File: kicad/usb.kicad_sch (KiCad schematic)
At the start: 46 parts, among them J2 HX PZ2.54-2X5P TP, U2 FSUSB42MUX, U3 USB2514B-I/M2, U4 AP22653W6-7, U5 TPD4EUSB30DQAR, U6 TPD4EUSB30DQAR, U7 TPD4EUSB30DQAR, X1 24MHz

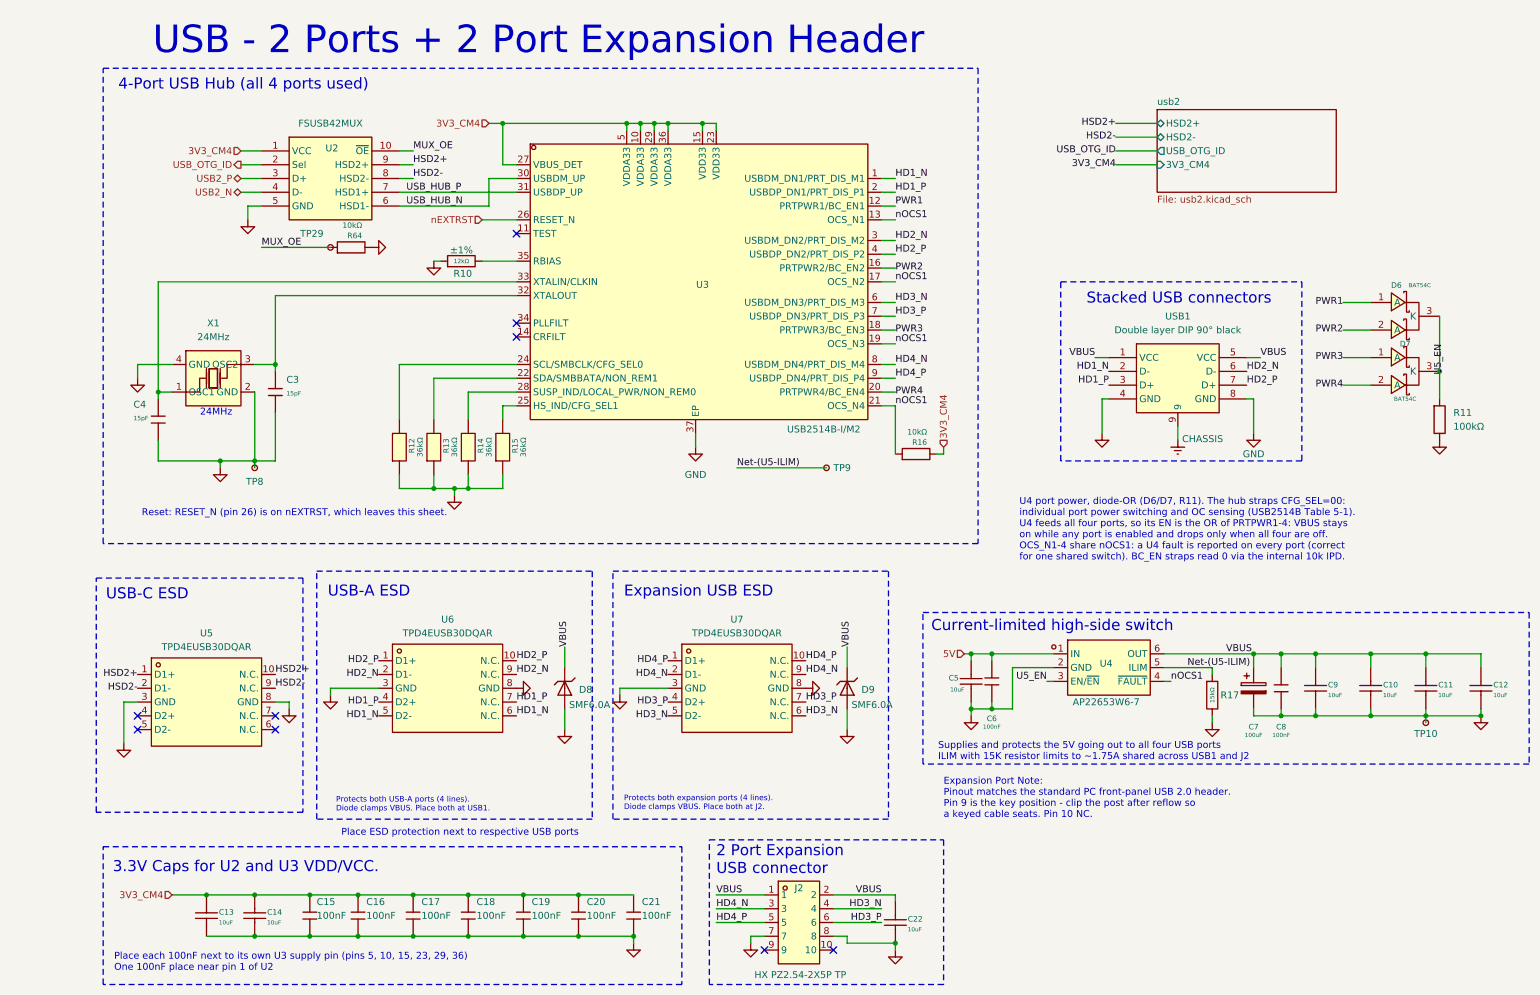
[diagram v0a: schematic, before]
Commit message: PCB: swap GPS and USB areas, drop J2 and hub ports 3/4, remap J4
- Remove expansion header J2 with C22, U7, D9 and D7; disable USB2514B
  ports 3 and 4 with 10k pull-ups (R94-R97) on their D-/D+ straps.
- Remap J4 GPIO pins so they route to the CM4 connector without
  crossovers (schematic labels, notes and PCB pad nets).
- Add decoupling caps C84 (U10) and C85 (U17); add HUB_CTRL net class.
- Move USB (USB1, USBC1, hub) to the top edge and GPS (U12, CN1, J7) to
  the bottom-left; R4/R5 move with the GPS group. First-pass placement,
  all USB and GPS copper removed for manual routing.
- Relabel bottom-edge silk text for the SMA connectors.
- README and usb-power sim note updated for the two-port hub.
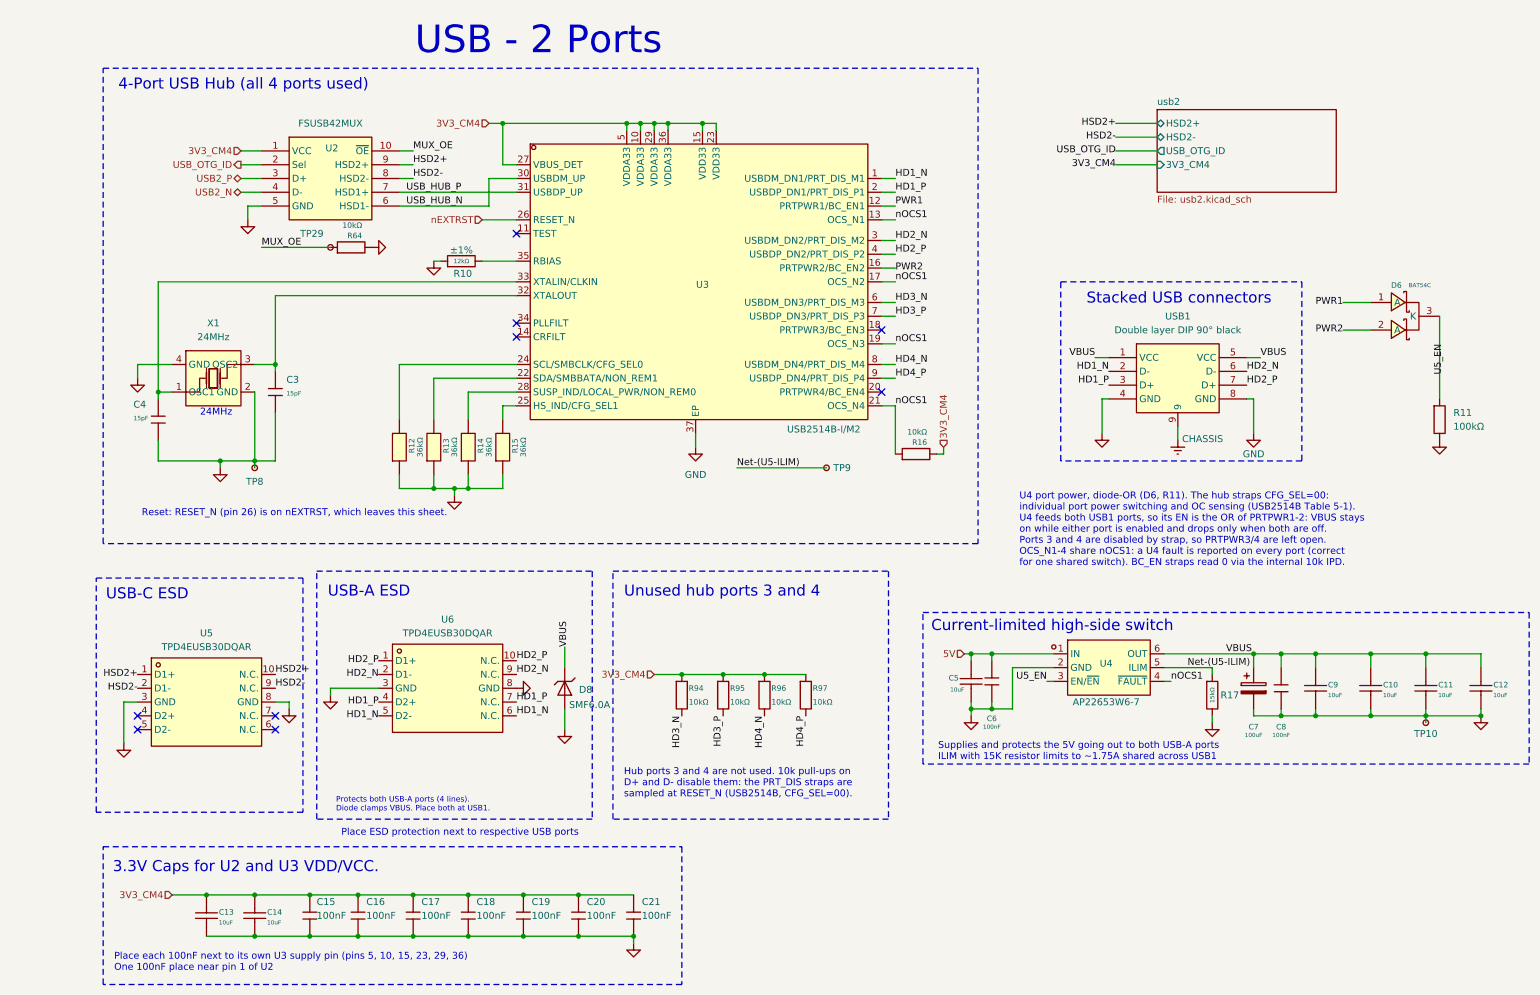
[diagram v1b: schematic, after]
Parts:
- removed C22: 10uF, MyPartsIPC:CAPC2012X145N, symbol MyParts:CL21B106KPQNNNE
- removed D7: BAT54C, MyPartsIPC:SOT95P280X110-3N, symbol MyParts:BAT54C
- removed D9: SMF6.0A, MyPartsIPC:SODFL3718X110N, symbol MyParts:SMF6.0A
- removed J2: HX PZ2.54-2X5P TP, MyParts:HDR-SMD_10P-P2.54-V-M-R2-C5-LS7.5, symbol MyParts:HXPZ2.54-2X5PTP
- removed U7: TPD4EUSB30DQAR, MyPartsIPC:SON50P100X250X60-10N, symbol MyParts:TPD4EUSB30DQAR
- added R94, R95, R96, R97: 10kΩ, MyPartsIPC:RESC1005X40N, symbol MyParts:0402WGF1002TCE
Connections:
- net 3V3_CM4: now also R94.1, R95.1, R96.1, R97.1
- net HD3_N: now also R94.2
- net HD3_P: now also R95.2
- net HD4_N: now also R96.2
- net HD4_P: now also R97.2
- net PWR3: no longer names the net of U3.18 (PRTPWR3/BC_EN3)
- net PWR4: no longer names the net of U3.20 (PRTPWR4/BC_EN4)
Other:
- note added: "Hub ports 3 and 4 are not used. 10k pull-ups on D+ and D- disable them: the PRT_DIS straps are sampled at RESET_N (USB2514B, CFG_SEL=00)."
- note added: "Supplies and protects the 5V going out to both USB-A ports ILIM with 15K resistor limits to ~1.75A shared across USB1"
- note added: "U4 port power, diode-OR (D6, R11). The hub straps CFG_SEL=00: individual port power switching and OC sensing (USB2514B Table 5-1). U4 feeds both USB1 ports, so its EN is the OR of PRTPWR1-2: VBUS stays on while either port is enabled and drops only when both are off. Ports 3 and 4 are disabled by strap, so PRTPWR3/4 are left open. OCS_N1-4 share nOCS1: a U4 fault is reported on every port (correc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"
- note added: "USB - 2 Ports"
- note added: "Unused hub ports 3 and 4"
- note removed: "2 Port Expansion USB connector"
- note removed: "Expansion Port Note: Pinout matches the standard PC front-panel USB 2.0 header. Pin 9 is the key position - clip the post after reflow so a keyed cable seats. Pin 10 NC."
- note removed: "Expansion USB ESD"
- note removed: "Protects both expansion ports (4 lines). Diode clamps VBUS. Place both at J2."
- note removed: "Supplies and protects the 5V going out to all four USB ports ILIM with 15K resistor limits to ~1.75A shared across USB1 and J2"
- note removed: "U4 port power, diode-OR (D6/D7, R11). The hub straps CFG_SEL=00: individual port power switching and OC sensing (USB2514B Table 5-1). U4 feeds all four ports, so its EN is the OR of PRTPWR1-4: VBUS stays on while any port is enabled and drops only when all four are off. OCS_N1-4 share nOCS1: a U4 fault is reported on every port (correct for one shared switch). BC_EN straps read 0 via the internal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"
- note removed: "USB - 2 Ports + 2 Port Expansion Header"

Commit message: PCB: route USB section and Ethernet, rework ESD flow-through wiring
USB:
- Connect C16 and nEXTRST (hub pin 26 to CM4 pin 100 under the module);
  re-route HS_IND to free pin 26; GND via for TP8.
- Restore 3D models dropped by API rotations; fix USBC1 power pads and
  peg holes and USB1 silkscreen (footprint fixes in parts).
- U5: HSD2 now flows through pins 4->7 and 5->6; pins 1, 2, 9, 10
  no-connect. U5 rotated and moved to suit.

Ethernet:
- U8/U9 N.C. pins carry the line (flow-through, like U6); their sheet
  symbol copy types those pins passive so ERC passes.
- Place U8/U9 in line with RJ1 pin gaps, C23 on the centre tap.
- Route all four pairs on ETH_100_OHM (0.11/0.13): outer-row pairs on
  F.Cu (EP2 hops under EP3), inner-row pairs via a B.Cu bundle, with the
  P/N and pair-order swaps done at the vias.
- LEDs on B.Cu to R18/R19 (positions swapped), CM4 GND pins 1/2, 7/8,
  13/14 via'd between the connector rows, RJ1 chassis pins tied.
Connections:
- net HSD2+: now also U2.8 (HSD2-), U5.4 (D2+), U5.7 (N.C.); no longer U2.9 (HSD2+), U5.1 (D1+), U5.10 (N.C.)
- net HSD2-: now also U2.9 (HSD2+), U5.5 (D2-), U5.6 (N.C.); no longer U2.8 (HSD2-), U5.2 (D1-), U5.9 (N.C.)
- net USB2_N: now also U2.3 (D+); no longer U2.4 (D-)
- net USB2_P: now also U2.4 (D-); no longer U2.3 (D+)
- net USB_HUB_N: now also U2.7 (HSD1+); no longer U2.6 (HSD1-)
- net USB_HUB_P: now also U2.6 (HSD1-); no longer U2.7 (HSD1+)
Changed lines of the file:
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@@
 	)
 	(rectangle
-		(start 17.78 119.38)
+		(start 13.97 119.38)
 		(end 55.88 162.56)
 		(stroke
@@
 	)
 	(no_connect
-		(at 25.4 144.78)
-	)
-	(no_connect
 		(at 162.56 85.09)
 	)
@@
 	)
 	(no_connect
-		(at 50.8 147.32)
-	)
-	(no_connect
-		(at 25.4 147.32)
-	)
-	(no_connect
 		(at 95.25 72.39)
 	)
 	(no_connect
-		(at 50.8 144.78)
-	)
-	(no_connect
 		(at 95.25 74.93)
 	)
@@
 	(wire
 		(pts
-			(xy 22.86 142.24) (xy 22.86 149.86)
+			(xy 15.24 142.24) (xy 15.24 149.86)
 		)
 		(stroke
@@
 	(wire
 		(pts
-			(xy 73.66 50.8) (xy 90.17 50.8)
-		)
-		(stroke
-			(width 0)
-			(type default)
-		)
-	)
-	(wire
-		(pts
 			(xy 173.99 95.25) (xy 173.99 96.52)
 		)
@@
 	(wire
 		(pts
-			(xy 53.34 142.24) (xy 53.34 143.51)
-		)
-		(stroke
-			(width 0)
-			(type default)
-		)
-	)
-	(wire
-		(pts
 			(xy 262.89 146.05) (xy 262.89 144.78)
 		)
@@
 	(wire
 		(pts
-			(xy 90.17 45.72) (xy 95.25 45.72)
-		)
-		(stroke
-			(width 0)
-			(type default)
-		)
-	)
-	(wire
-		(pts
-			(xy 73.66 48.26) (xy 95.25 48.26)
-		)
-		(stroke
-			(width 0)
-			(type default)
-		)
-	)
-	(wire
-		(pts
 			(xy 86.36 185.42) (xy 96.52 185.42)
 		)
@@
 	(wire
 		(pts
-			(xy 90.17 50.8) (xy 90.17 45.72)
-		)
-		(stroke
-			(width 0)
-			(type default)
-		)
-	)
-	(wire
-		(pts
 			(xy 60.96 139.7) (xy 60.96 140.97)
 		)
@@
 	(wire
 		(pts
-			(xy 50.8 142.24) (xy 53.34 142.24)
-		)
-		(stroke
-			(width 0)
-			(type default)
-		)
-	)
-	(wire
-		(pts
 			(xy 48.26 58.42) (xy 60.96 58.42)
 		)
@@
 	(wire
 		(pts
-			(xy 25.4 142.24) (xy 22.86 142.24)
+			(xy 25.4 142.24) (xy 15.24 142.24)
 		)
 		(stroke
@@
 		)
 	)
-	(label "USB_HUB_N"
+	(label "USB_HUB_P"
 		(at 74.93 50.8 0)
 		(effects
@@
 		)
 	)
-	(label "HSD2+"
+	(label "HSD2-"
 		(at 76.2 43.18 0)
 		(effects
@@
 	)
 	(label "HSD2+"
-		(at 25.4 137.16 180)
+		(at 25.4 144.78 180)
 		(effects
 			(font
@@
 	)
 	(label "HSD2-"
-		(at 25.4 139.7 180)
+		(at 25.4 147.32 180)
 		(effects
 			(font
@@
 		)
 	)
-	(label "HSD2+"
-		(at 50.8 137.16 0)
-		(effects
-			(font
-				(size 1.27 1.27)
-			)
-			(justify left bottom)
-		)
-	)
 	(label "HD1_N"
 		(at 165.1 45.72 0)
@@
 		)
 	)
-	(label "HSD2-"
+	(label "HSD2+"
 		(at 76.2 45.72 0)
 		(effects
@@
 		)
 	)
-	(label "HSD2-"
-		(at 50.8 139.7 0)
-		(effects
-			(font
-				(size 1.27 1.27)
-			)
-			(justify left bottom)
-		)
-	)
 	(label "HD2_N"
 		(at 165.1 57.15 0)
@@
 		)
 	)
-	(label "USB_HUB_P"
+	(label "USB_HUB_N"
 		(at 74.93 48.26 0)
 		(effects
@@
 		)
 	)
-	(hierarchical_label "USB2_N"
+	(hierarchical_label "USB2_P"
 		(shape bidirectional)
 		(at 44.45 48.26 180)
@@
 		)
 	)
-	(hierarchical_label "USB2_P"
+	(hierarchical_label "USB2_N"
 		(shape bidirectional)
 		(at 44.45 45.72 180)
@@
 	(symbol
 		(lib_id "power:GND")
-		(at 53.34 143.51 0)
+		(at 50.8 142.24 90)
 		(unit 1)
 		(body_style 1)
@@
 		(in_pos_files yes)
 		(dnp no)
-		(fields_autoplaced yes)
 		(property "Reference" "#PWR084"
-			(at 53.34 149.86 0)
+			(at 54.61 142.24 90)
 			(hide yes)
 			(show_name no)
@@
 		)
 		(property "Value" "GND"
-			(at 53.34 148.59 0)
+			(at 46.99 142.24 90)
 			(hide yes)
 			(show_name no)
@@
 		)
 		(property "Footprint" ""
-			(at 53.34 143.51 0)
+			(at 50.8 142.24 90)
 			(hide yes)
 			(show_name no)
@@
 		)
 		(property "Datasheet" ""
-			(at 53.34 143.51 0)
+			(at 50.8 142.24 90)
 			(hide yes)
 			(show_name no)
@@
 	(symbol
 		(lib_id "power:GND")
-		(at 22.86 149.86 0)
+		(at 15.24 149.86 0)
 		(unit 1)
 		(body_style 1)
@@
 		(fields_autoplaced yes)
 		(property "Reference" "#PWR083"
-			(at 22.86 156.21 0)
+			(at 15.24 156.21 0)
 			(hide yes)
 			(show_name no)
@@
 		)
 		(property "Value" "GND"
-			(at 22.86 154.94 0)
+			(at 15.24 154.94 0)
 			(hide yes)
 			(show_name no)
@@
 		)
 		(property "Footprint" ""
-			(at 22.86 149.86 0)
+			(at 15.24 149.86 0)
 			(hide yes)
 			(show_name no)
@@
 		)
 		(property "Datasheet" ""
-			(at 22.86 149.86 0)
+			(at 15.24 149.86 0)
 			(hide yes)
 			(show_name no)
@@
 		)
 		(property "Description" "Power symbol creates a global label with name \"GND\" , ground"
-			(at 22.86 149.86 0)
+			(at 15.24 149.86 0)
 			(hide yes)
 			(show_name no)
@@
 		)
 	)
+	(wire
+		(pts
+			(xy 73.66 48.26) (xy 87.63 48.26)
+		)
+		(stroke
+			(width 0)
+			(type default)
+		)
+	)
+	(wire
+		(pts
+			(xy 87.63 48.26) (xy 87.63 45.72)
+		)
+		(stroke
+			(width 0)
+			(type default)
+		)
+	)
+	(wire
+		(pts
+			(xy 87.63 45.72) (xy 95.25 45.72)
+		)
+		(stroke
+			(width 0)
+			(type default)
+		)
+	)
+	(wire
+		(pts
+			(xy 73.66 50.8) (xy 92.71 50.8)
+		)
+		(stroke
+			(width 0)
+			(type default)
+		)
+	)
+	(wire
+		(pts
+			(xy 92.71 50.8) (xy 92.71 48.26)
+		)
+		(stroke
+			(width 0)
+			(type default)
+		)
+	)
+	(wire
+		(pts
+			(xy 92.71 48.26) (xy 95.25 48.26)
+		)
+		(stroke
+			(width 0)
+			(type default)
+		)
+	)
+	(no_connect
+		(at 25.4 137.16)
+	)
+	(no_connect
+		(at 50.8 137.16)
+	)
+	(no_connect
+		(at 25.4 139.7)
+	)
+	(no_connect
+		(at 50.8 139.7)
+	)
+	(label "HSD2+"
+		(at 50.8 144.78 0)
+		(effects
+			(font
+				(size 1.27 1.27)
+			)
+			(justify left bottom)
+		)
+	)
+	(label "HSD2-"
+		(at 50.8 147.32 0)
+		(effects
+			(font
+				(size 1.27 1.27)
+			)
+			(justify left bottom)
+		)
+	)
